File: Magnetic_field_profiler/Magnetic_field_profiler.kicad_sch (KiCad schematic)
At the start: 66 parts, among them J1 USB_B_Micro, J2 Screw_Terminal_01x02, J3 Conn_01x04_Socket, J4 Conn_01x04_Socket, Q1 BSS123, SW1 SW_SPDT, U1 STM32F103C8Tx, U2 TP6841S6, U3 MCP23S17, U4 DRV8825, U5 DRV8825, Y1 Crystal_GND24

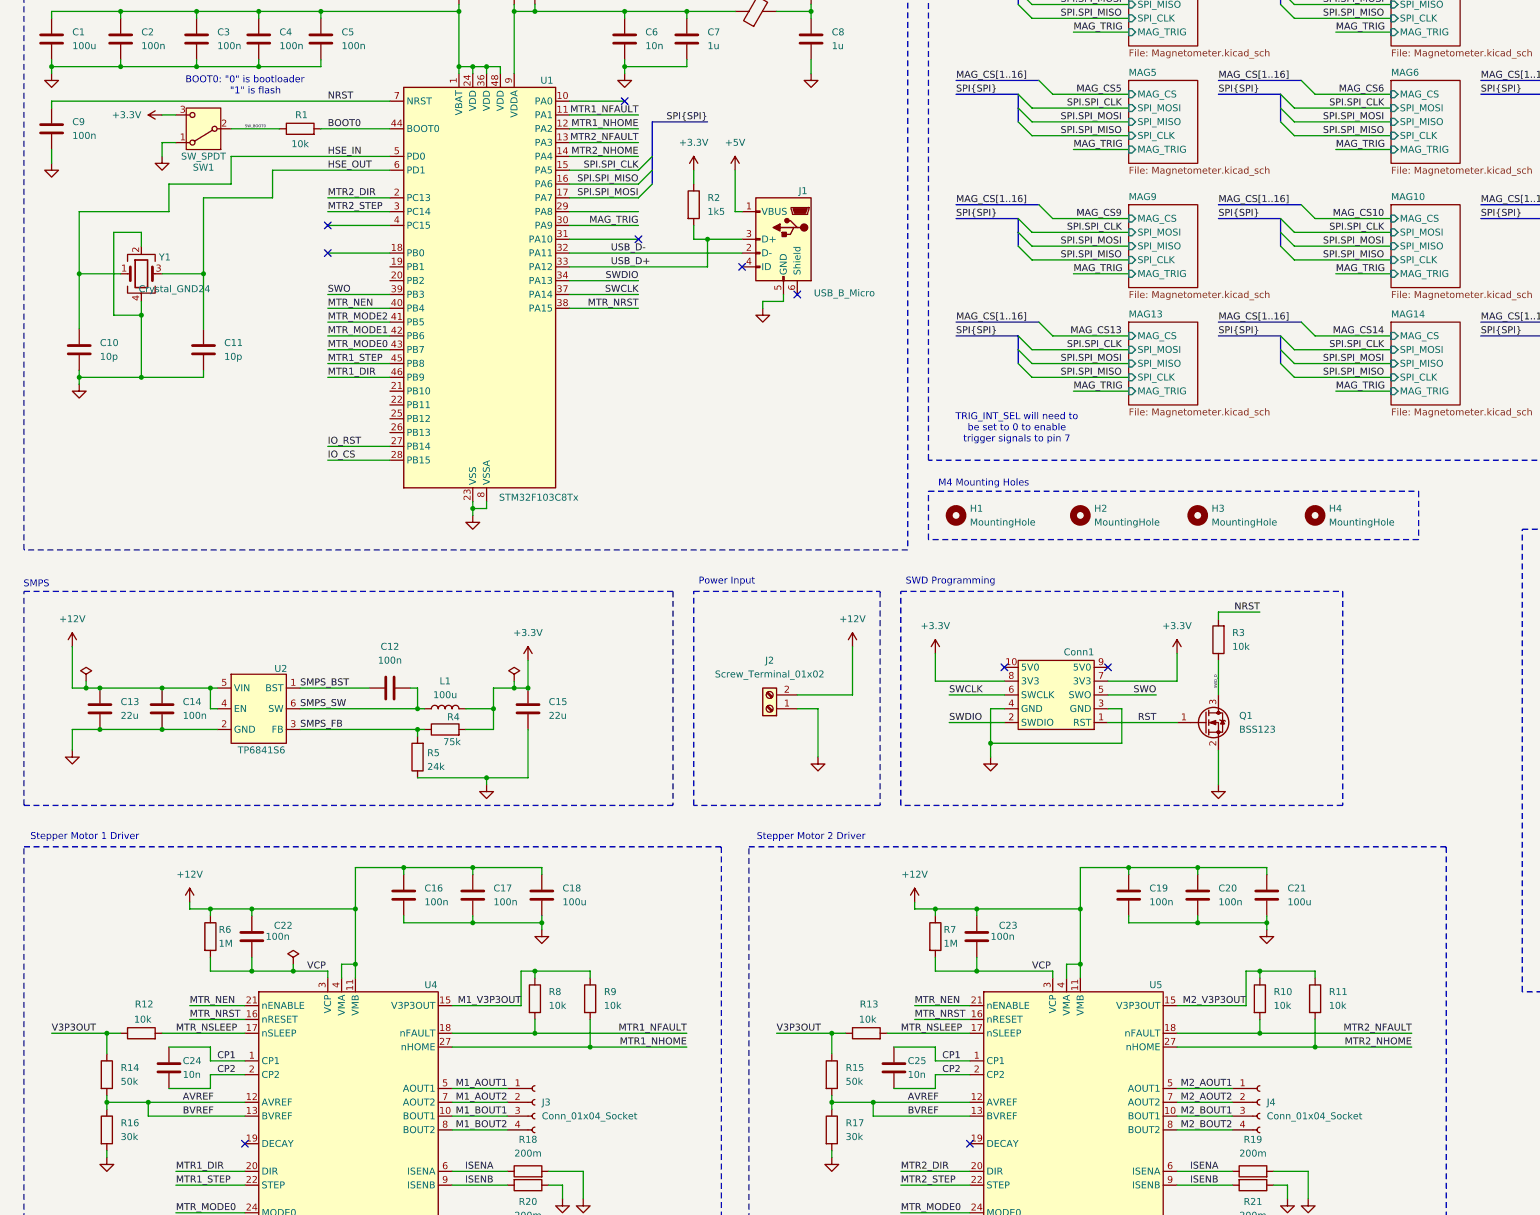
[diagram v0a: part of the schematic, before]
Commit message: Swapping MCU IOs and defining netclasses
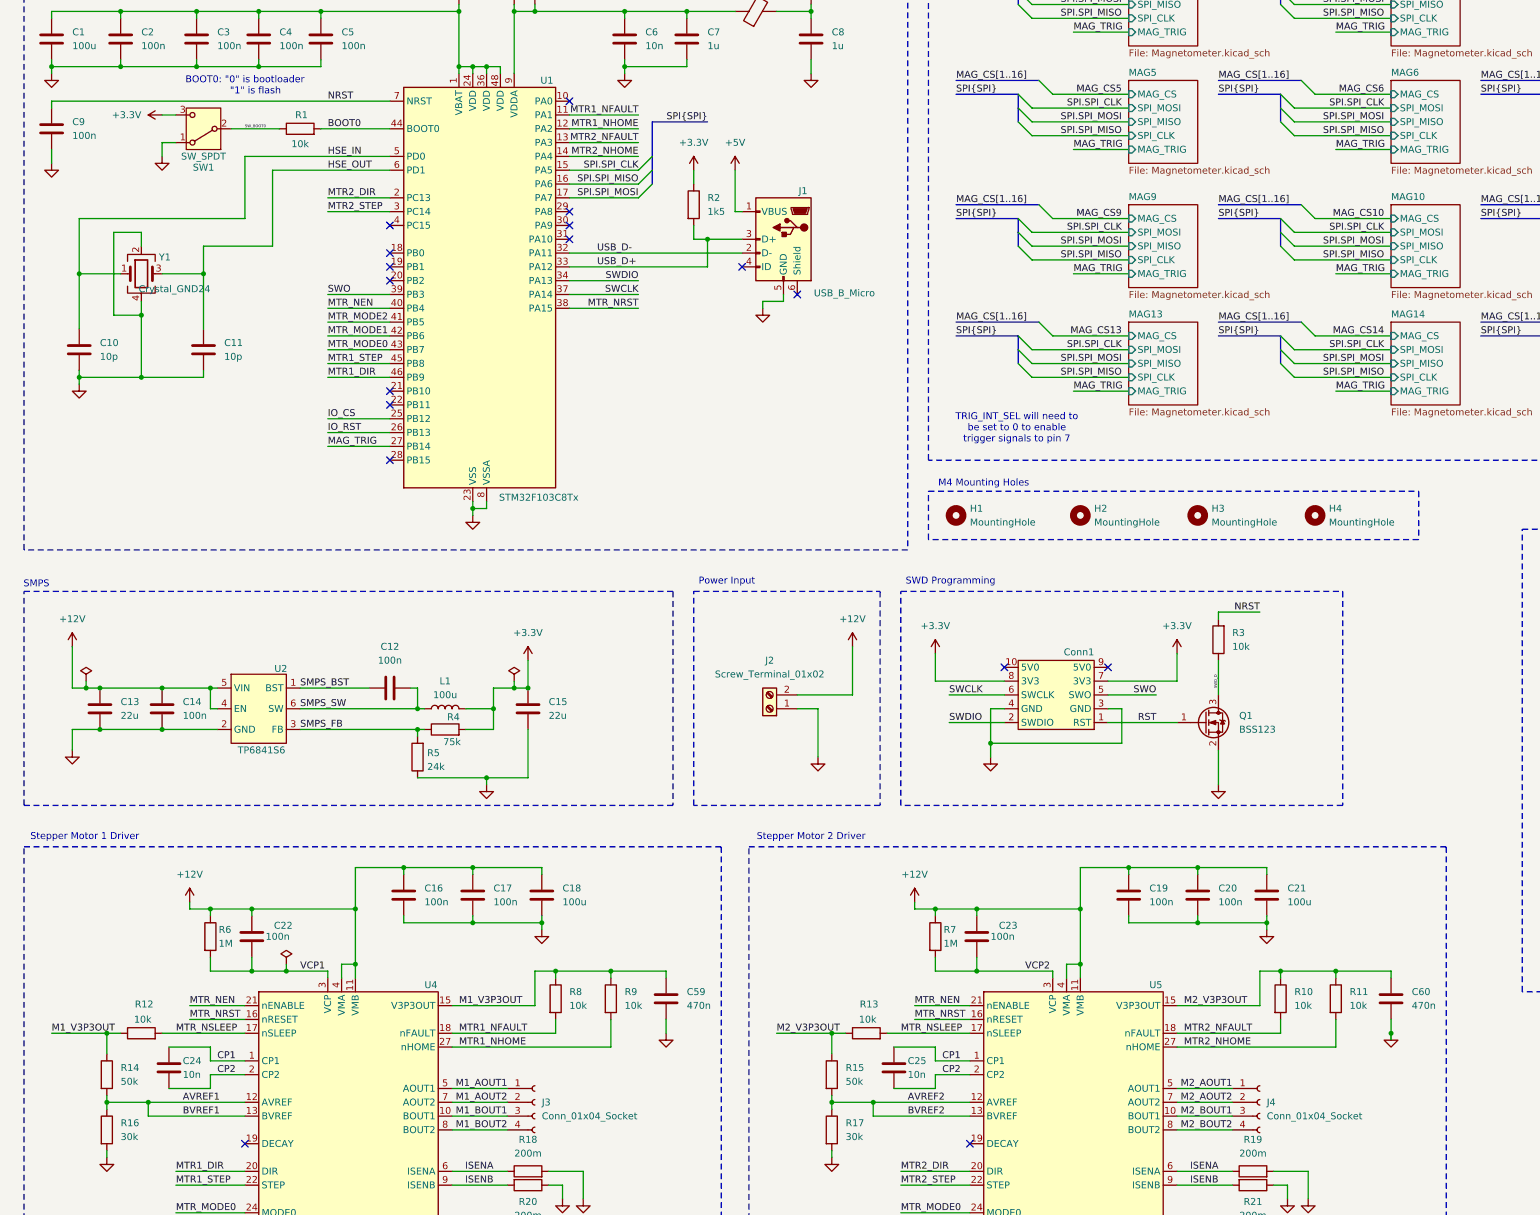
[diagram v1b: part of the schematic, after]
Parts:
- added C59, C60: 470n, Capacitor_SMD:C_0402_1005Metric, symbol Device:C
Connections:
- net GND: now also C59.2, C60.2
- net IO_CS: now also U1.25 (PB12); no longer U1.28 (PB15)
- net IO_RST: now also U1.26 (PB13); no longer U1.27 (PB14)
- net M1_V3P3OUT: now also R12.1, R14.1, C59.1
- net M2_V3P3OUT: now also R13.1, R15.1, C60.1
- net MAG_TRIG: now also U1.27 (PB14); no longer U1.30 (PA9)
- net AVREF renamed AVREF1
- net AVREF1: no longer R15.2, R17.1, U5.12 (AVREF), U5.13 (BVREF)
- removed net V3P3OUT: R12.1, R13.1, R14.1, R15.1
- net VCP renamed VCP1
- net VCP1: no longer C23.2, R7.2, U5.3 (VCP)
- new net AVREF2: R15.2, R17.1, U5.12 (AVREF), U5.13 (BVREF)
- new net VCP2: C23.2, R7.2, U5.3 (VCP)
- no-connect marks 12 -> 19
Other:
- moved on the sheet: R10, R11

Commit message: ???
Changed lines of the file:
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@@
 	)
 	(junction
+		(at 207.01 209.55)
+		(diameter 0)
+		(color 0 0 0 0)
+	)
+	(junction
 		(at 233.68 190.5)
 		(diameter 0)
@@
 	)
 	(junction
-		(at 269.24 220.98)
-		(diameter 0)
-		(color 0 0 0 0)
-	)
-	(junction
 		(at 31.75 157.48)
 		(diameter 0)
@@
 	(wire
 		(pts
+			(xy 207.01 207.01) (xy 207.01 209.55)
+		)
+		(stroke
+			(width 0)
+			(type default)
+		)
+	)
+	(wire
+		(pts
 			(xy 80.01 266.7) (xy 80.01 267.97)
 		)
@@
 	(wire
 		(pts
-			(xy 269.24 220.98) (xy 269.24 222.25)
-		)
-		(stroke
-			(width 0)
-			(type default)
-		)
-	)
-	(wire
-		(pts
 			(xy 102.87 123.19) (xy 102.87 124.46)
 		)
@@
 					(unit 1)
 				)
+			)
+		)
+	)
+	(symbol
+		(lib_id "power:PWR_FLAG")
+		(at 207.01 207.01 0)
+		(unit 1)
+		(exclude_from_sim no)
+		(in_bom yes)
+		(on_board yes)
+		(dnp no)
+		(fields_autoplaced yes)
+		(property "Reference" "#FLG05"
+			(at 207.01 205.105 0)
+			(effects
+				(font
+					(size 1.27 1.27)
+				)
+				(hide yes)
+			)
+		)
+		(property "Value" "PWR_FLAG"
+			(at 207.01 201.93 0)
+			(effects
+				(font
+					(size 1.27 1.27)
+				)
+				(hide yes)
+			)
+		)
+		(property "Footprint" ""
+			(at 207.01 207.01 0)
+			(effects
+				(font
+					(size 1.27 1.27)
+				)
+				(hide yes)
+			)
+		)
+		(property "Datasheet" "~"
+			(at 207.01 207.01 0)
+			(effects
+				(font
+					(size 1.27 1.27)
+				)
+				(hide yes)
+			)
+		)
+		(property "Description" "Special symbol for telling ERC where power comes from"
+			(at 207.01 207.01 0)
+			(effects
+				(font
+					(size 1.27 1.27)
+				)
+				(hide yes)
+			)
+		)
+		(pin "1"
+		)
+		(instances
+			(project "Magnetic_field_profiler"
+				(path "/a3309886-ab27-4f3f-a056-7adffbf55c8a"
+					(reference "#FLG05")
+					(unit 1)
+				)

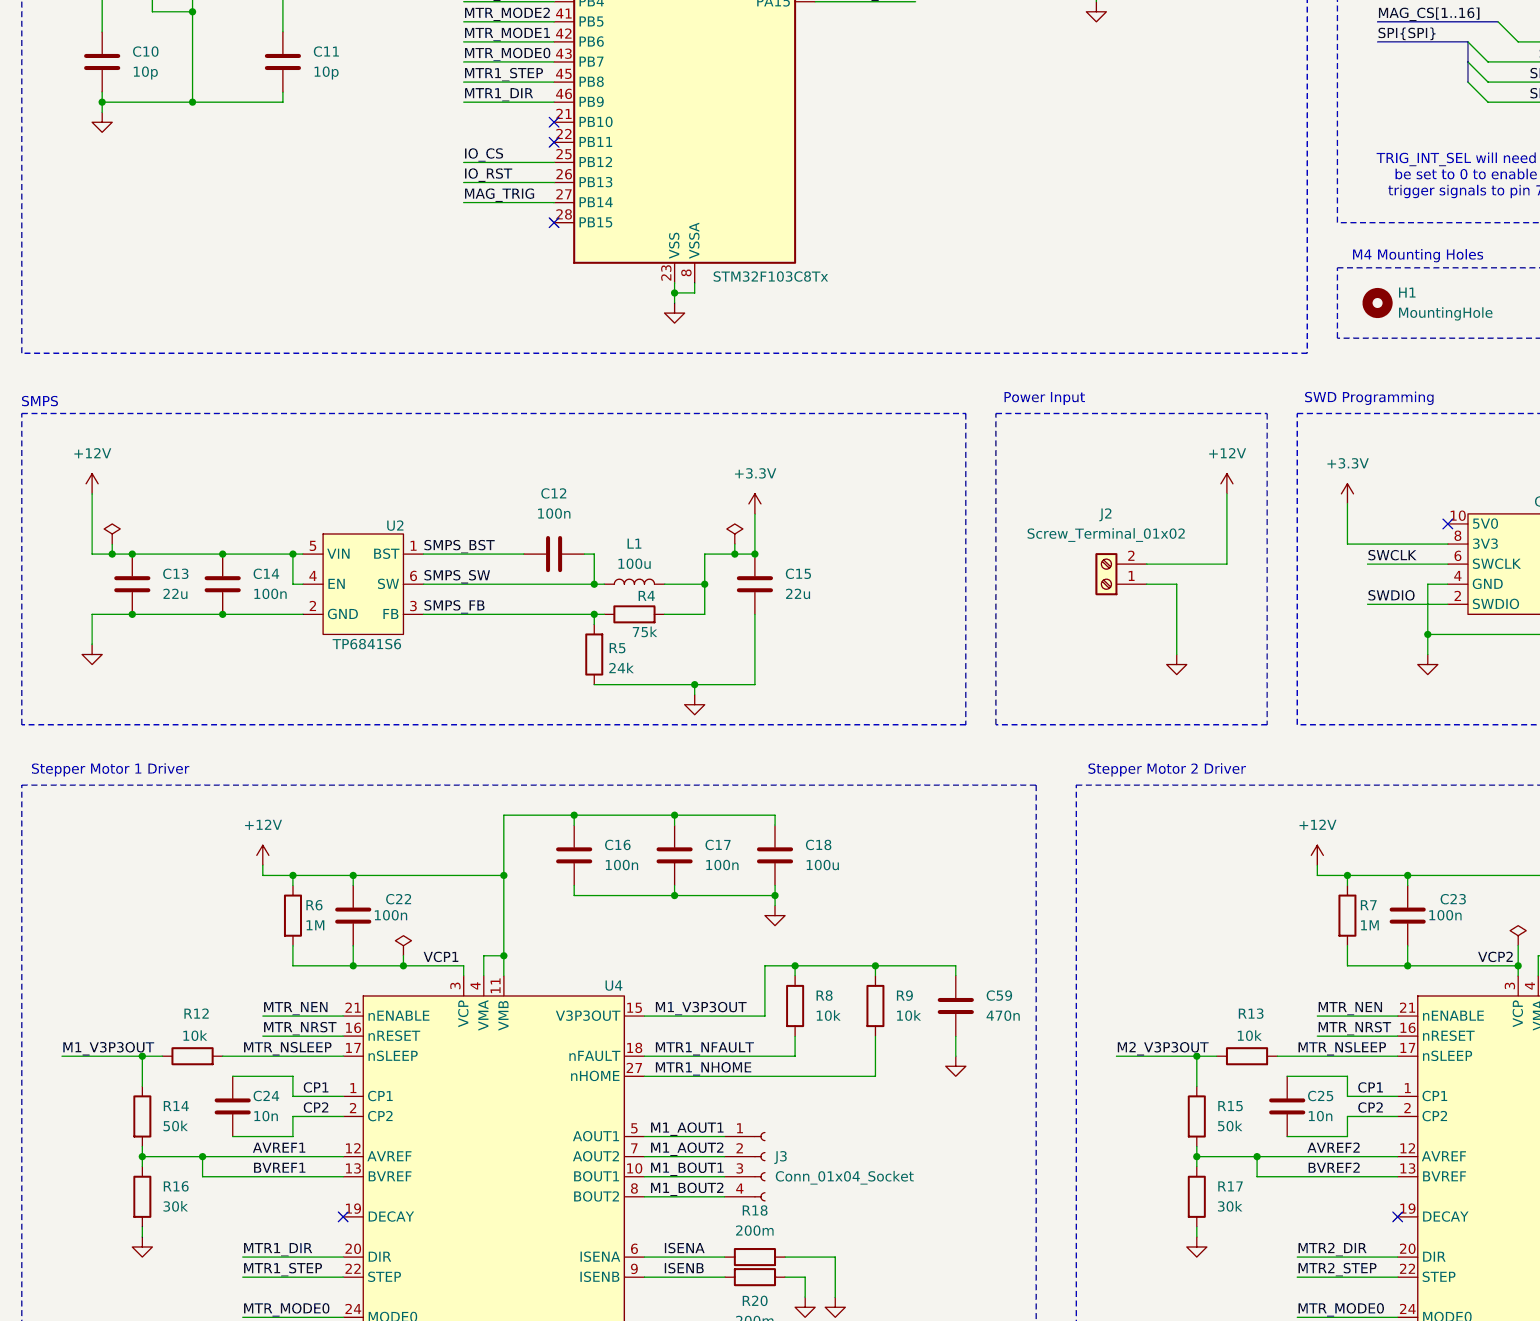
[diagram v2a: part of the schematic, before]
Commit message: Added status LEDs, began updating netclass trace widths
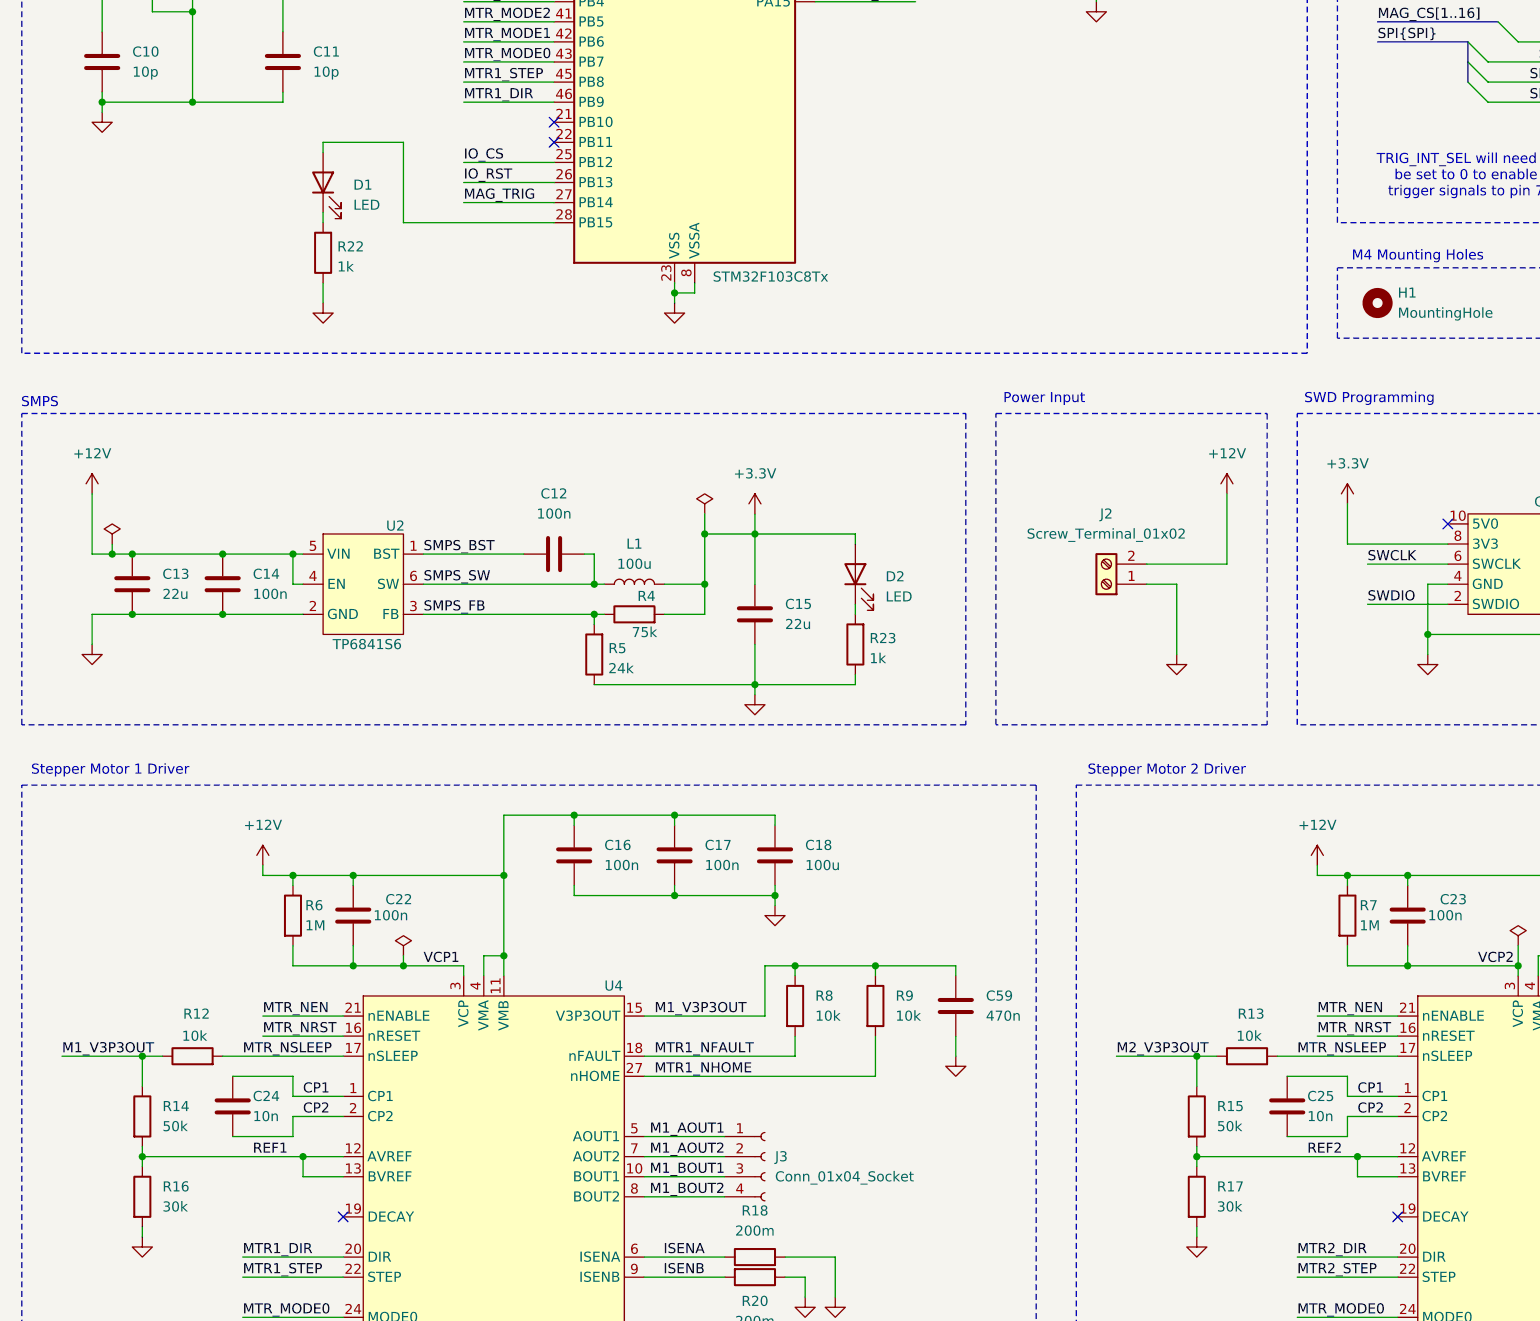
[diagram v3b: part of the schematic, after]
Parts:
- added D1, D2: LED, symbol Device:LED
- added R22, R23: 1k, Resistor_SMD:R_0402_1005Metric, symbol Device:R
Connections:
- net +3.3V: now also D2.2 (A)
- net GND: now also R22.1, R23.1
- net at U1.28 (PB15): now also D1.2 (A)
- net AVREF1 renamed REF1
- net AVREF2 renamed REF2
- new net: D2.1 (K), R23.2
- new net: D1.1 (K), R22.2
- no-connect marks 19 -> 18
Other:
- moved on the sheet: C15

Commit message: BOM Information Update
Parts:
- D1: value LED -> STATUS_LED; footprint (none) -> LED_SMD:LED_0805_2012Metric; Distributor Link (none) -> https://www.digikey.com/en/products/detail/w%C3%BCrth-elekt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; Manufacturer (none) -> Würth Elektronik; Manufacturer Part Number (none) -> 150080VS75000
- D2: value LED -> PWR_LED; footprint (none) -> LED_SMD:LED_0805_2012Metric; Distributor Link (none) -> https://www.digikey.com/en/products/detail/w%C3%BCrth-elekt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; Manufacturer (none) -> Würth Elektronik; Manufacturer Part Number (none) -> 150080RS75000
- J1: Distributor Link (none) -> https://www.digikey.com/en/products/detail/w%C3%BCrth-elekt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; Manufacturer (none) -> Wurth Elektronik; Manufacturer Part Number (none) -> 629105150521
- J3, J4: Distributor Link (none) -> https://www.digikey.com/en/products/detail/jst-sales-americ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; Manufacturer (none) -> JST Sales America Inc.; Manufacturer Part Number (none) -> S4B-PH-K-S
- SW1: Distributor Link (none) -> https://www.digikey.com/en/products/detail/omron-electronic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; Manufacturer (none) -> Omron Electronics Inc-EMC Div; Manufacturer Part Number (none) -> B3F-1000
- U1: Distributor Link (none) -> https://www.digikey.com/en/products/detail/stmicroelectroni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; Manufacturer (none) -> STMicroelectronics; Manufacturer Part Number (none) -> STM32F103C8T6TR
- U3: Distributor Link (none) -> https://www.digikey.com/en/products/detail/microchip-techno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; Manufacturer (none) -> Microchip Technology; Manufacturer Part Number (none) -> MCP23S17T-E/SS
- U4, U5: Distributor Link (none) -> https://www.digikey.com/en/products/detail/texas-instrument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; Manufacturer (none) -> Texas Instruments; Manufacturer Part Number (none) -> DRV8825PWPR
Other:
- note added: "IO Expander"
